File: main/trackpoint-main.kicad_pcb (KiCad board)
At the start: 2 copper layers, 27.5 x 24 mm, 19 parts

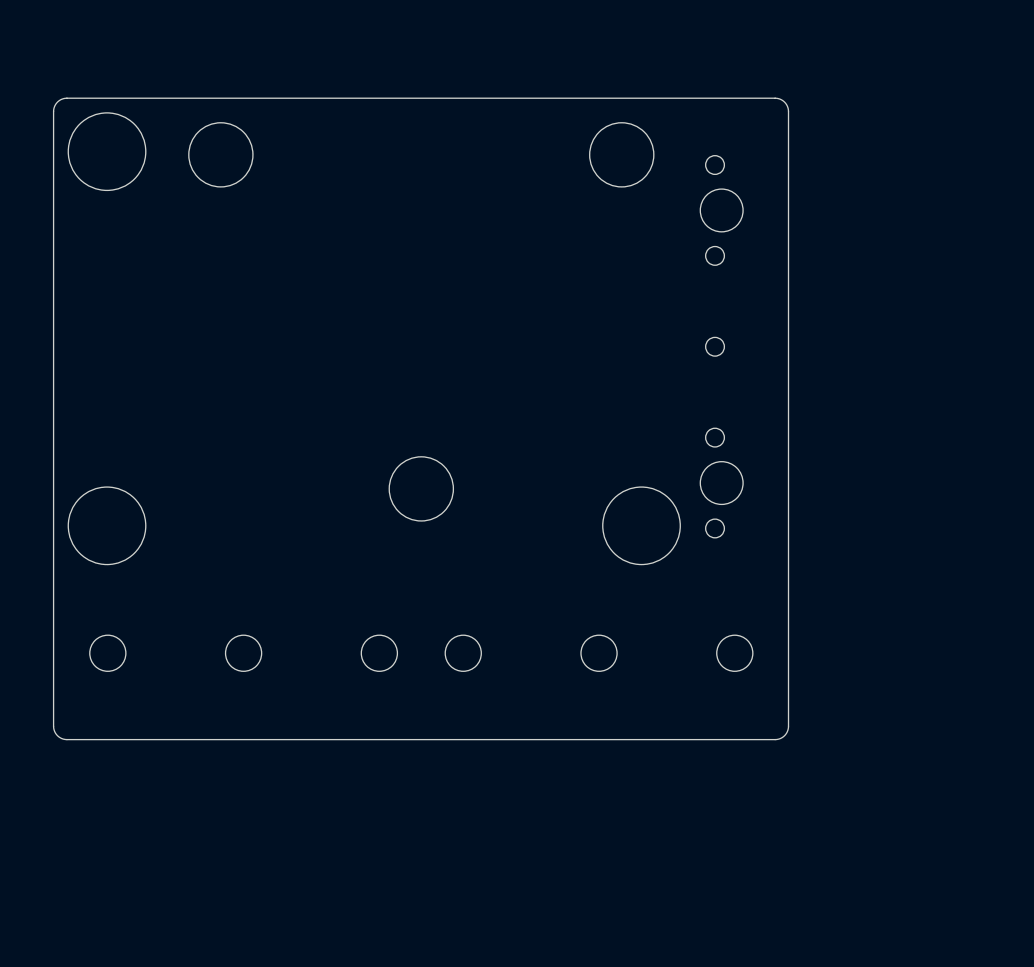
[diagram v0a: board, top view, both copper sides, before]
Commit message: Add 2 microswitches and a male pogo pin header.
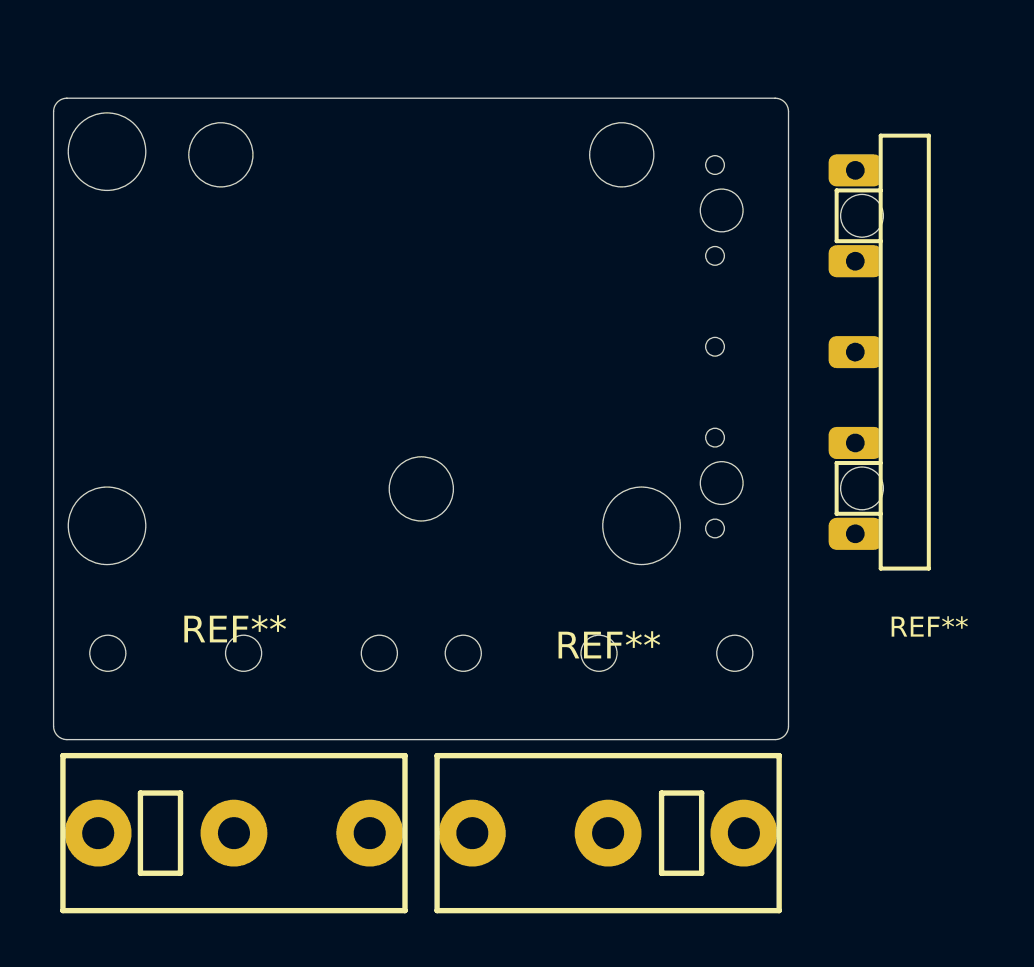
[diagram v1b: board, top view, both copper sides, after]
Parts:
- added REF**: VAL**, ugl:UHK_Male_Pogo_Pin_v2, F.Cu at (225.0, 133.0)
- added REF**: CMI126603D08, ugl:CMI126603D08, F.Cu at (213.0, 151.0)
- added REF**: CMI126603D08, ugl:CMI126603D08, F.Cu at (199.0, 151.0)
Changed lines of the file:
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@@
     (tracks 0)
     (zones 0)
-    (modules 19)
+    (modules 22)
     (nets 1)
   )
@@
     (uvia_drill 0.127)
   )
+  (module ugl:UHK_Male_Pogo_Pin_v2 (layer F.Cu)
+    (at 225 133)
+    (attr virtual)
+    (fp_text reference REF** (at 0 10.3) (layer F.SilkS)
+      (effects (font (size 0.75 0.75) (thickness 0.15)))
+    )
+    (fp_text value VAL** (at 0 -9.95 180) (layer F.SilkS) hide
+      (effects (font (size 0.75 0.75) (thickness 0.15)))
+    )
+    (fp_line (start 2.5 -9.1) (end 2.5 9.3) (layer Cmts.User) (width 0.15))
+    (fp_line (start 0 9.3) (end 2.5 9.3) (layer Cmts.User) (width 0.15))
+    (fp_line (start -1.8 8.1) (end -1.8 -8.1) (layer F.SilkS) (width 0.15))
+    (fp_line (start 0 -9.1) (end 2.5 -9.1) (layer Cmts.User) (width 0.15))
+    (fp_line (start 2.5 -7.3) (end 3 -7.3) (layer Cmts.User) (width 0.15))
+    (fp_line (start 2.5 -6.3) (end 3 -6.3) (layer Cmts.User) (width 0.15))
+    (fp_arc (start 3.1 -6.8) (end 3.1 -6.3) (angle -180) (layer Cmts.User) (width 0.15))
+    (fp_line (start 2.5 -2.9) (end 3 -2.9) (layer Cmts.User) (width 0.15))
+    (fp_line (start 2.5 -3.9) (end 3 -3.9) (layer Cmts.User) (width 0.15))
+    (fp_arc (start 3.1 -3.4) (end 3.1 -2.9) (angle -180) (layer Cmts.User) (width 0.15))
+    (fp_line (start 2.5 0.5) (end 3 0.5) (layer Cmts.User) (width 0.15))
+    (fp_line (start 2.5 -0.5) (end 3 -0.5) (layer Cmts.User) (width 0.15))
+    (fp_arc (start 3.1 0) (end 3.1 0.5) (angle -180) (layer Cmts.User) (width 0.15))
+    (fp_line (start 2.5 3.9) (end 3 3.9) (layer Cmts.User) (width 0.15))
+    (fp_line (start 2.5 2.9) (end 3 2.9) (layer Cmts.User) (width 0.15))
+    (fp_arc (start 3.1 3.4) (end 3.1 3.9) (angle -180) (layer Cmts.User) (width 0.15))
+    (fp_line (start 2.5 7.3) (end 3 7.3) (layer Cmts.User) (width 0.15))
+    (fp_line (start 2.5 6.3) (end 3 6.3) (layer Cmts.User) (width 0.15))
+    (fp_arc (start 3.1 6.8) (end 3.1 7.3) (angle -180) (layer Cmts.User) (width 0.15))
+    (fp_line (start 0 9.3) (end 0 -9.1) (layer Cmts.User) (width 0.15))
+    (fp_line (start -1.8 -8.1) (end 0 -8.1) (layer F.SilkS) (width 0.15))
+    (fp_line (start 0 8.1) (end -1.8 8.1) (layer F.SilkS) (width 0.15))
+    (fp_line (start -1.8 -6.05) (end -3.45 -6.05) (layer F.SilkS) (width 0.15))
+    (fp_line (start -3.45 -6.05) (end -3.45 -4.15) (layer F.SilkS) (width 0.15))
+    (fp_line (start -3.45 -4.15) (end -1.8 -4.15) (layer F.SilkS) (width 0.15))
+    (fp_line (start -1.8 6.05) (end -3.45 6.05) (layer F.SilkS) (width 0.15))
+    (fp_line (start -3.45 6.05) (end -3.45 4.15) (layer F.SilkS) (width 0.15))
+    (fp_line (start -3.45 4.15) (end -1.8 4.15) (layer F.SilkS) (width 0.15))
+    (fp_line (start 0 8.1) (end 0 -8.1) (layer F.SilkS) (width 0.15))
+    (pad 1 thru_hole roundrect (at -2.75 -6.8) (size 2 1.2) (drill 0.7) (layers *.Cu *.Mask) (roundrect_rratio 0.25)
+      (clearance 0.0762))
+    (pad 2 thru_hole roundrect (at -2.75 -3.4) (size 2 1.2) (drill 0.7) (layers *.Cu *.Mask) (roundrect_rratio 0.25)
+      (clearance 0.0762))
+    (pad 3 thru_hole roundrect (at -2.75 0) (size 2 1.2) (drill 0.7) (layers *.Cu *.Mask) (roundrect_rratio 0.25))
+    (pad 4 thru_hole roundrect (at -2.75 3.4) (size 2 1.2) (drill 0.7) (layers *.Cu *.Mask) (roundrect_rratio 0.25)
+      (clearance 0.0762))
+    (pad 5 thru_hole roundrect (at -2.75 6.8) (size 2 1.2) (drill 0.7) (layers *.Cu *.Mask) (roundrect_rratio 0.25)
+      (clearance 0.0762))
+    (pad "" np_thru_hole circle (at -2.5 -5.1) (size 1.6 1.6) (drill 1.6) (layers *.Cu *.Mask)
+      (clearance 0.00254))
+    (pad "" np_thru_hole circle (at -2.5 5.1 180) (size 1.6 1.6) (drill 1.6) (layers *.Cu *.Mask)
+      (clearance 0.00254))
+  )
+  (module ugl:CMI126603D08 (layer F.Cu)
+    (at 213 151 180)
+    (fp_text reference REF** (at 0 7) (layer F.SilkS)
+      (effects (font (size 1 1) (thickness 0.15)))
+    )
+    (fp_text value CMI126603D08 (at 0 8.8) (layer F.Fab)
+      (effects (font (size 1 1) (thickness 0.15)))
+    )
+    (fp_line (start 6.4 -2.9) (end -6.4 -2.9) (layer F.SilkS) (width 0.2))
+    (fp_line (start -6.4 -2.9) (end -6.4 2.9) (layer F.SilkS) (width 0.2))
+    (fp_line (start -6.4 2.9) (end 6.4 2.9) (layer F.SilkS) (width 0.2))
+    (fp_line (start 6.4 -2.9) (end 6.4 2.9) (layer F.SilkS) (width 0.2))
+    (fp_line (start -3.5 -1.5) (end -2 -1.5) (layer F.SilkS) (width 0.2))
+    (fp_line (start -2 -1.5) (end -2 1.5) (layer F.SilkS) (width 0.2))
+    (fp_line (start -2 1.5) (end -3.5 1.5) (layer F.SilkS) (width 0.2))
+    (fp_line (start -3.5 1.5) (end -3.5 -1.5) (layer F.SilkS) (width 0.2))
+    (pad 1 thru_hole circle (at -5.08 0 180) (size 2.5 2.5) (drill 1.2) (layers *.Cu *.Mask))
+    (pad 2 thru_hole circle (at 0 0 180) (size 2.5 2.5) (drill 1.2) (layers *.Cu *.Mask))
+    (pad 3 thru_hole circle (at 5.08 0 180) (size 2.5 2.5) (drill 1.2) (layers *.Cu *.Mask))
+  )
+  (module ugl:CMI126603D08 (layer F.Cu)
+    (at 199 151)
+    (fp_text reference REF** (at 0 -7.6) (layer F.SilkS)
+      (effects (font (size 1 1) (thickness 0.15)))
+    )
+    (fp_text value CMI126603D08 (at 0 8.8) (layer F.Fab)
+      (effects (font (size 1 1) (thickness 0.15)))
+    )
+    (fp_line (start -3.5 1.5) (end -3.5 -1.5) (layer F.SilkS) (width 0.2))
+    (fp_line (start -2 1.5) (end -3.5 1.5) (layer F.SilkS) (width 0.2))
+    (fp_line (start -2 -1.5) (end -2 1.5) (layer F.SilkS) (width 0.2))
+    (fp_line (start -3.5 -1.5) (end -2 -1.5) (layer F.SilkS) (width 0.2))
+    (fp_line (start 6.4 -2.9) (end 6.4 2.9) (layer F.SilkS) (width 0.2))
+    (fp_line (start -6.4 2.9) (end 6.4 2.9) (layer F.SilkS) (width 0.2))
+    (fp_line (start -6.4 -2.9) (end -6.4 2.9) (layer F.SilkS) (width 0.2))
+    (fp_line (start 6.4 -2.9) (end -6.4 -2.9) (layer F.SilkS) (width 0.2))
+    (pad 3 thru_hole circle (at 5.08 0) (size 2.5 2.5) (drill 1.2) (layers *.Cu *.Mask))
+    (pad 2 thru_hole circle (at 0 0) (size 2.5 2.5) (drill 1.2) (layers *.Cu *.Mask))
+    (pad 1 thru_hole circle (at -5.08 0) (size 2.5 2.5) (drill 1.2) (layers *.Cu *.Mask))
+  )
   (module UGL:hole_2.9000000953674316mm locked (layer F.Cu)

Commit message: Finalize the positions of the microswitches.
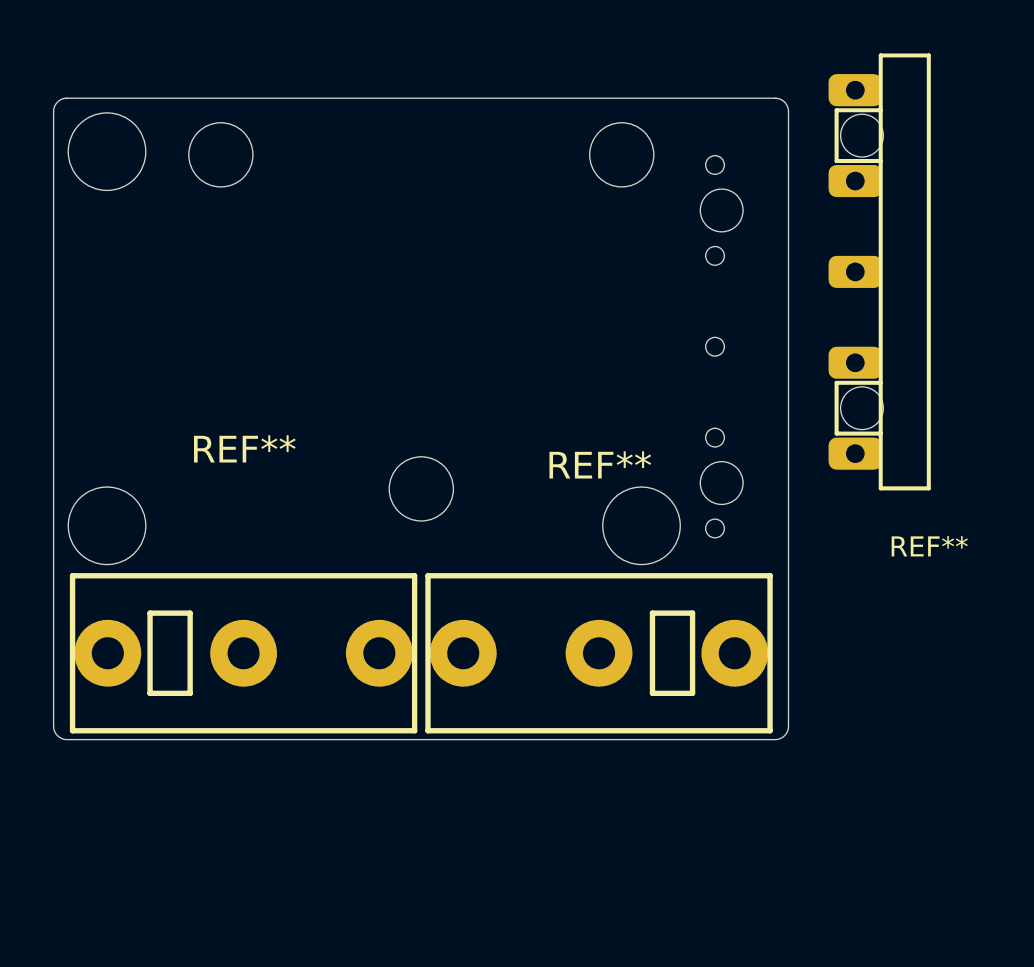
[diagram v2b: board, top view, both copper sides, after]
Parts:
- removed the ? at (212.7, 144.3)
- removed the ? at (204.4, 144.3)
- removed the ? at (194.3, 144.3)
- removed the ? at (199.4, 144.3)
- removed the ? at (207.6, 144.3)
- removed the ? at (217.7, 144.3)
- removed the REF** at (213.0, 151.0)
- removed the REF** at (199.0, 151.0)
- added REF**: CMI126603D08, ugl:CMI126603D08, F.Cu at (199.4, 144.3)
- added REF**: CMI126603D08, ugl:CMI126603D08, F.Cu at (212.7, 144.3)
- moved REF** 3.00 mm to (225.0, 130.0)

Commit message: Move the pogo pin connector to its final position.
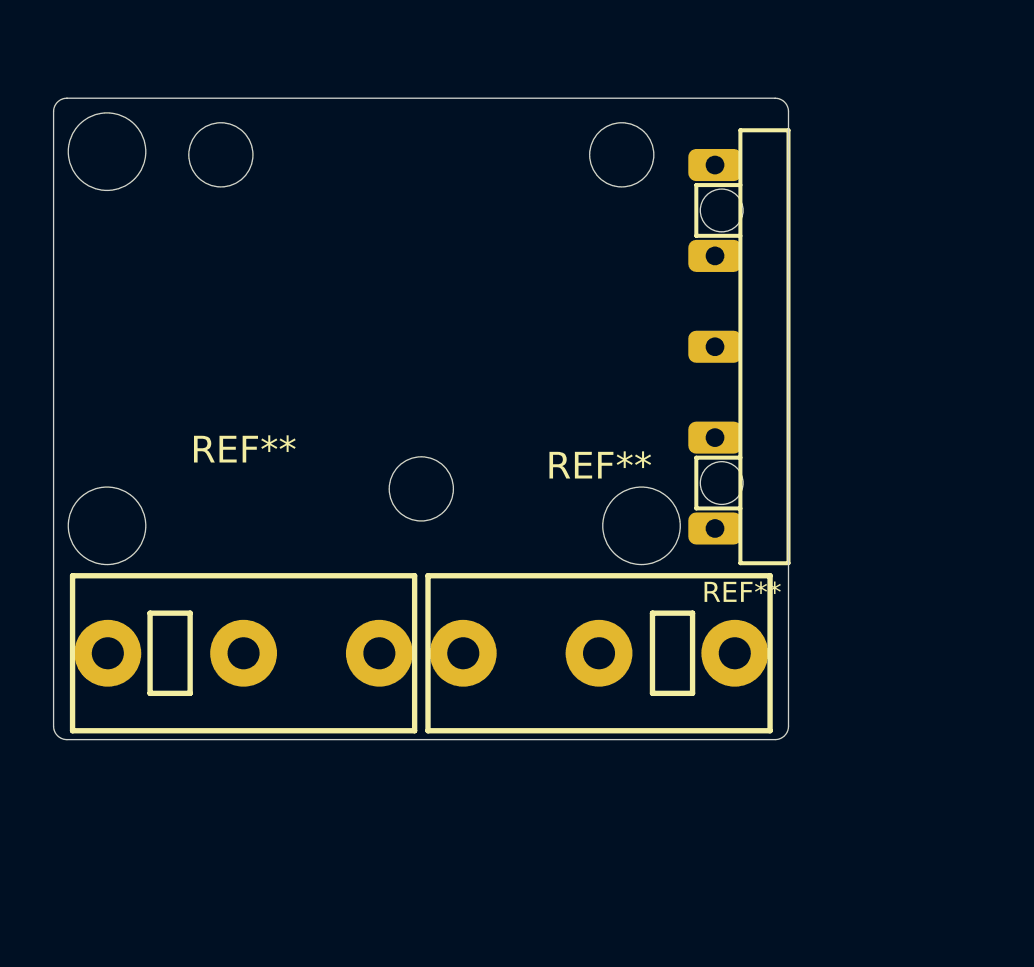
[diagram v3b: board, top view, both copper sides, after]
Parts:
- removed the ? at (217.2, 127.7)
- removed the ? at (217.2, 137.9)
- removed the ? at (217.0, 136.2)
- removed the ? at (217.0, 129.4)
- removed the ? at (217.0, 126.0)
- removed the ? at (217.0, 132.8)
- removed the ? at (217.0, 139.6)
- moved REF** 5.95 mm to (219.8, 132.8)

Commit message: Add version number and PCB ID text for the main board.
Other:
- board text added: "PCB ID: trackpoint_main_0.1.0"
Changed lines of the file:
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@@
   (general
     (thickness 1.6)
-    (drawings 8)
+    (drawings 9)
     (tracks 0)
     (zones 0)
@@
   )
   (page A3)
+  (title_block
+    (title "UHK Trackpoint Module")
+    (rev 0.1.0)
+    (company "Ultimate Gadget Laboratories Kft.")
+  )
   (layers
     (0 F.Cu signal)
@@
       (clearance 0.00001))
   )
+  (gr_text "PCB ID: trackpoint_main_0.1.0" (at 206.1 146.5) (layer B.SilkS)
+    (effects (font (size 1 1) (thickness 0.2)) (justify mirror))
+  )
   (gr_arc (start 192.75 124.000007) (end 192.75 123.5) (angle -90.00451968) (layer Edge.Cuts) (width 0.01))
